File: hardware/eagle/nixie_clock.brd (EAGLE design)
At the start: 273.1 x 130.8 mm, 39 parts, among them IC1 74141N, IC10 74141N, IC11 7477N, IC12 74141N, IC13 7477N, IC14 74AC11238, IC2 7477N, IC4 74141N, IC5 7477N, IC6 74141N, IC7 7477N, IC8 74141N, IC9 7477N

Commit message: First board
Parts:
- removed IC14: 74AC11238, 74ac-logic:DIL16
- added IC3: 74141N, 74xx-eu:DIL16
- added J1_180V, J1_180V1: 22-27-2021-02, con-molex:6410-02
- IC10, IC12, IC4, IC6, IC8: value 74141N -> 7477N; device 74xx-eu:DIL16 -> 74xx-eu:DIL14
- IC11, IC5, IC7, IC9: value 7477N -> 74141N; device 74xx-eu:DIL14 -> 74xx-eu:DIL16
- IC13: value 7477N -> 74AC11238; device 74xx-eu:DIL14 -> 74ac-logic:DIL16
- moved C13 254.8 mm to (118.7, 16.5), turned to 90 degrees
- moved R2 248.9 mm to (5.08, 69.2), turned to 180 degrees
- moved R3 248.9 mm to (5.08, 65.4), turned to 180 degrees
- moved R4 248.9 mm to (5.08, 61.6), turned to 180 degrees
- moved R5 248.9 mm to (5.08, 57.8), turned to 180 degrees
- moved R6 248.9 mm to (5.08, 54.0), turned to 180 degrees
- moved C9 221.2 mm to (41.9, 43.2)
- moved GPIO_HEADER1 220.5 mm to (91.4, 7.62)
- moved C11 217.4 mm to (21.6, 43.2)
- moved IC11 215.8 mm to (22.9, 50.8)
- moved C10 208.9 mm to (59.7, 27.9), turned to 180 degrees
- moved IC13 205.0 mm to (128.3, 14.6), turned to 90 degrees
- moved C12 203.2 mm to (41.9, 27.9), turned to 180 degrees
- moved IN-8-5 198.1 mm to (52.1, 66.0)
- moved IN-8-6 192.8 mm to (35.6, 66.0)
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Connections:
- net +5V: now also IC10.4, IC11.5, IC12.4, IC13.11, IC13.12, IC3.5, IC4.4, IC5.5, IC6.4, IC7.5, IC8.4, IC9.5, J1_180V1.1; no longer IC10.5, IC11.4, IC12.5, IC13.4, IC14.11, IC14.12, IC4.5, IC5.4, IC6.5, IC7.4, IC8.5, IC9.4
- net GND: now also IC10.11, IC11.12, IC12.11, IC13.10, IC13.4, IC13.9, IC3.12, IC4.11, IC5.12, IC6.11, IC7.12, IC8.11, IC9.12, J1_180V.1, J1_180V1.2; no longer IC10.12, IC11.11, IC12.12, IC13.11, IC14.10, IC14.4, IC14.9, IC4.12, IC5.11, IC6.12, IC7.11, IC8.12, IC9.11
- net N$1: now also IN-8-1.A; no longer IN-8-2.A
- net N$10: now also IN-8-1.9; no longer IN-8-2.9
- net N$11: now also IN-8-1.0; no longer IN-8-2.0
- net N$16: now also IC13.16; no longer IC14.16
- net N$17: now also IC10.6, IC12.6, IC4.6, IC6.6, IC8.6; no longer IC11.6, IC13.6, IC5.6, IC7.6, IC9.6
- net N$18: now also IN-8-2.A; no longer IN-8-1.A
- net N$19: now also IC3.15, IN-8-2.1; no longer IC4.15, IN-8-1.1
- net N$2: now also IN-8-1.1; no longer IN-8-2.1
- net N$20: now also IC3.8, IN-8-2.2; no longer IC4.8, IN-8-1.2
- net N$21: now also IC3.9, IN-8-2.3; no longer IC4.9, IN-8-1.3
- net N$22: now also IC3.13, IN-8-2.4; no longer IC4.13, IN-8-1.4
- net N$23: now also IC3.14, IN-8-2.5; no longer IC4.14, IN-8-1.5
- net N$24: now also IC3.11, IN-8-2.6; no longer IC4.11, IN-8-1.6
- net N$25: now also IC3.10, IN-8-2.7; no longer IC4.10, IN-8-1.7
- net N$26: now also IC3.1, IN-8-2.8; no longer IC4.1, IN-8-1.8
- net N$27: now also IC3.2, IN-8-2.9; no longer IC4.2, IN-8-1.9
- net N$28: now also IC3.16, IN-8-2.0; no longer IC4.16, IN-8-1.0
- net N$29: now also IC3.3, IC4.14; no longer IC4.3, IC5.14
- net N$3: now also IN-8-1.2; no longer IN-8-2.2
- net N$30: now also IC3.6, IC4.13; no longer IC4.6, IC5.13
- net N$31: now also IC3.7, IC4.9; no longer IC4.7, IC5.9
- net N$32: now also IC3.4, IC4.8; no longer IC4.4, IC5.8
- net N$33: now also IC13.1, IC4.12, IC4.3; no longer IC14.1, IC5.12, IC5.3
- net N$34: now also IC5.15; no longer IC6.15
- net N$35: now also IC5.8; no longer IC6.8
- net N$36: now also IC5.9; no longer IC6.9
- net N$37: now also IC5.13; no longer IC6.13
- net N$38: now also IC5.14; no longer IC6.14
- net N$39: now also IC5.11; no longer IC6.11
- net N$4: now also IN-8-1.3; no longer IN-8-2.3
- net N$40: now also IC5.10; no longer IC6.10
- net N$41: now also IC5.1; no longer IC6.1
- net N$42: now also IC5.2; no longer IC6.2
- net N$43: now also IC5.16; no longer IC6.16
- net N$44: now also IC5.3, IC6.14; no longer IC6.3, IC7.14
- net N$45: now also IC5.6, IC6.13; no longer IC6.6, IC7.13
- net N$46: now also IC5.7, IC6.9; no longer IC6.7, IC7.9
- net N$47: now also IC5.4, IC6.8; no longer IC6.4, IC7.8
- net N$48: now also IC13.2, IC6.12, IC6.3; no longer IC14.2, IC7.12, IC7.3
- net N$49: now also IC7.15; no longer IC8.15
- net N$5: now also IN-8-1.4; no longer IN-8-2.4
- net N$50: now also IC7.8; no longer IC8.8
- net N$51: now also IC7.9; no longer IC8.9
- net N$52: now also IC7.13; no longer IC8.13
- net N$53: now also IC7.14; no longer IC8.14
- net N$54: now also IC7.11; no longer IC8.11
- net N$55: now also IC7.10; no longer IC8.10
- net N$56: now also IC7.1; no longer IC8.1
- net N$57: now also IC7.2; no longer IC8.2
- net N$58: now also IC7.16; no longer IC8.16
- net N$59: now also IC7.3, IC8.14; no longer IC8.3, IC9.14
- net N$6: now also IN-8-1.5; no longer IN-8-2.5
- net N$60: now also IC7.6, IC8.13; no longer IC8.6, IC9.13
- net N$61: now also IC7.7, IC8.9; no longer IC8.7, IC9.9
- net N$62: now also IC7.4, IC8.8; no longer IC8.4, IC9.8
- net N$63: now also IC13.3, IC8.12, IC8.3; no longer IC14.3, IC9.12, IC9.3
- net N$64: now also IC9.15; no longer IC10.15
- net N$65: now also IC9.8; no longer IC10.8
- net N$66: now also IC9.9; no longer IC10.9
- net N$67: now also IC9.13; no longer IC10.13
- net N$68: now also IC9.14; no longer IC10.14
- net N$69: now also IC9.11; no longer IC10.11
- net N$7: now also IN-8-1.6; no longer IN-8-2.6
- net N$70: now also IC9.10; no longer IC10.10
- net N$71: now also IC9.1; no longer IC10.1
- net N$72: now also IC9.2; no longer IC10.2
- net N$73: now also IC9.16; no longer IC10.16
- net N$74: now also IC10.14, IC9.3; no longer IC10.3, IC11.14
- net N$75: now also IC10.13, IC9.6; no longer IC10.6, IC11.13
- net N$76: now also IC10.9, IC9.7; no longer IC10.7, IC11.9
- net N$77: now also IC10.8, IC9.4; no longer IC10.4, IC11.8
- net N$78: now also IC10.12, IC10.3, IC13.5; no longer IC11.12, IC11.3, IC14.5
- net N$79: now also IC11.15; no longer IC12.15
- net N$8: now also IN-8-1.7; no longer IN-8-2.7
- net N$80: now also IC11.8; no longer IC12.8
- net N$81: now also IC11.9; no longer IC12.9
- net N$82: now also IC11.13; no longer IC12.13
- net N$83: now also IC11.14; no longer IC12.14
- net N$84: now also IC11.11; no longer IC12.11
- net N$85: now also IC11.10; no longer IC12.10
- net N$86: now also IC11.1; no longer IC12.1
- net N$87: now also IC11.2; no longer IC12.2
- net N$88: now also IC11.16; no longer IC12.16
- net N$89: now also IC11.3, IC12.14; no longer IC12.3, IC13.14
- net N$9: now also IN-8-1.8; no longer IN-8-2.8
- net N$90: now also IC11.6, IC12.13; no longer IC12.6, IC13.13
- net N$91: now also IC11.7, IC12.9; no longer IC12.7, IC13.9
- net N$92: now also IC11.4, IC12.8; no longer IC12.4, IC13.8
- net N$93: now also IC12.12, IC12.3, IC13.6; no longer IC13.12, IC13.3, IC14.6
- net N$94: now also IC10.5, IC12.5, IC4.5, IC6.5, IC8.5; no longer IC11.5, IC13.5, IC5.5, IC7.5, IC9.5
- net N$95: now also IC10.2, IC12.2, IC4.2, IC6.2, IC8.2; no longer IC11.2, IC13.2, IC5.2, IC7.2, IC9.2
- net N$96: now also IC10.1, IC12.1, IC4.1, IC6.1, IC8.1; no longer IC11.1, IC13.1, IC5.1, IC7.1, IC9.1
- net N$97: now also IC13.15; no longer IC14.15
- net N$98: now also IC13.14; no longer IC14.14
- net N$99: now also IC13.13; no longer IC14.13
- net VCC: now also J1_180V.2
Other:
- board size 273.1 x 130.8 mm -> 138.4 x 74.9 mm

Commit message: Updated eagle project
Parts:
- removed J1_180V1: 22-27-2021-02, con-molex:6410-02
- added J1_5V1: 22-27-2021-02, con-molex:6410-02
- R1, R2, R3, R4, R5, R6: device resistor:0204/5 -> resistor:0207/15
- moved R1 65.9 mm to (33.0, 12.7), turned to 270 degrees
- moved R2 61.5 mm to (29.2, 12.7), turned to 270 degrees
- moved R3 56.5 mm to (25.4, 12.7), turned to 270 degrees
- moved J1_180V 53.6 mm to (48.3, 14.0), turned to 0 degrees
- moved R4 51.6 mm to (21.6, 12.7), turned to 270 degrees
- moved R5 46.8 mm to (17.8, 12.7), turned to 270 degrees
- moved R6 42.2 mm to (14.0, 12.7), turned to 270 degrees
- moved C12 25.4 mm to (16.5, 27.9), turned to 0 degrees
- moved C10 24.1 mm to (35.6, 27.9), turned to 0 degrees
- moved IN-8-6 22.9 mm to (12.7, 66.0)
- moved IC12 19.0 mm to (17.8, 35.6)
- moved IN-8-5 19.0 mm to (33.0, 66.0)
- moved IC10 17.8 mm to (36.8, 35.6)
- moved C8 15.2 mm to (62.2, 27.9), turned to 0 degrees
- moved C6 14.0 mm to (81.3, 27.9), turned to 0 degrees
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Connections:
- new net N$108: C1.2, C10.2, C11.2, C12.2, C13.2, C2.2, C3.2, C4.2, C5.2, C6.2, C7.2, C8.2, C9.2, IC1.5, IC10.4, IC11.5, IC12.4, IC13.11, IC13.12, IC2.4, IC3.5, IC4.4, IC5.5, IC6.4, IC7.5, IC8.4, IC9.5, J1_5V1.2
- net +5V: no longer C1.2, C10.2, C11.2, C12.2, C13.2, C2.2, C3.2, C4.2, C5.2, C6.2, C7.2, C8.2, C9.2, IC1.5, IC10.4, IC11.5, IC12.4, IC13.11, IC13.12, IC2.4, IC3.5, IC4.4, IC5.5, IC6.4, IC7.5, IC8.4, IC9.5, J1_180V1.1
- net GND: now also J1_5V1.1; no longer J1_180V1.2
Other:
- board size 138.4 x 74.9 mm -> 141 x 74.9 mm

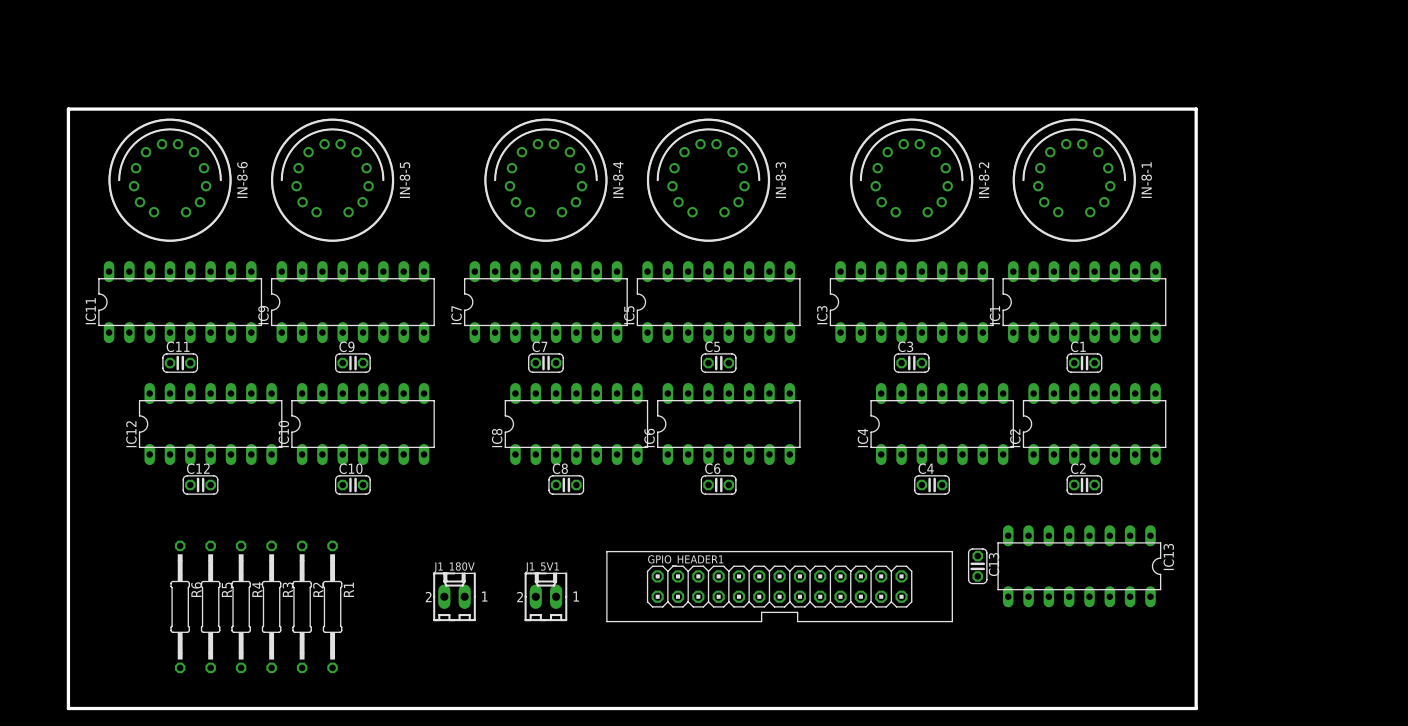
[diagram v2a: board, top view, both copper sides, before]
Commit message: External nixie tubes design
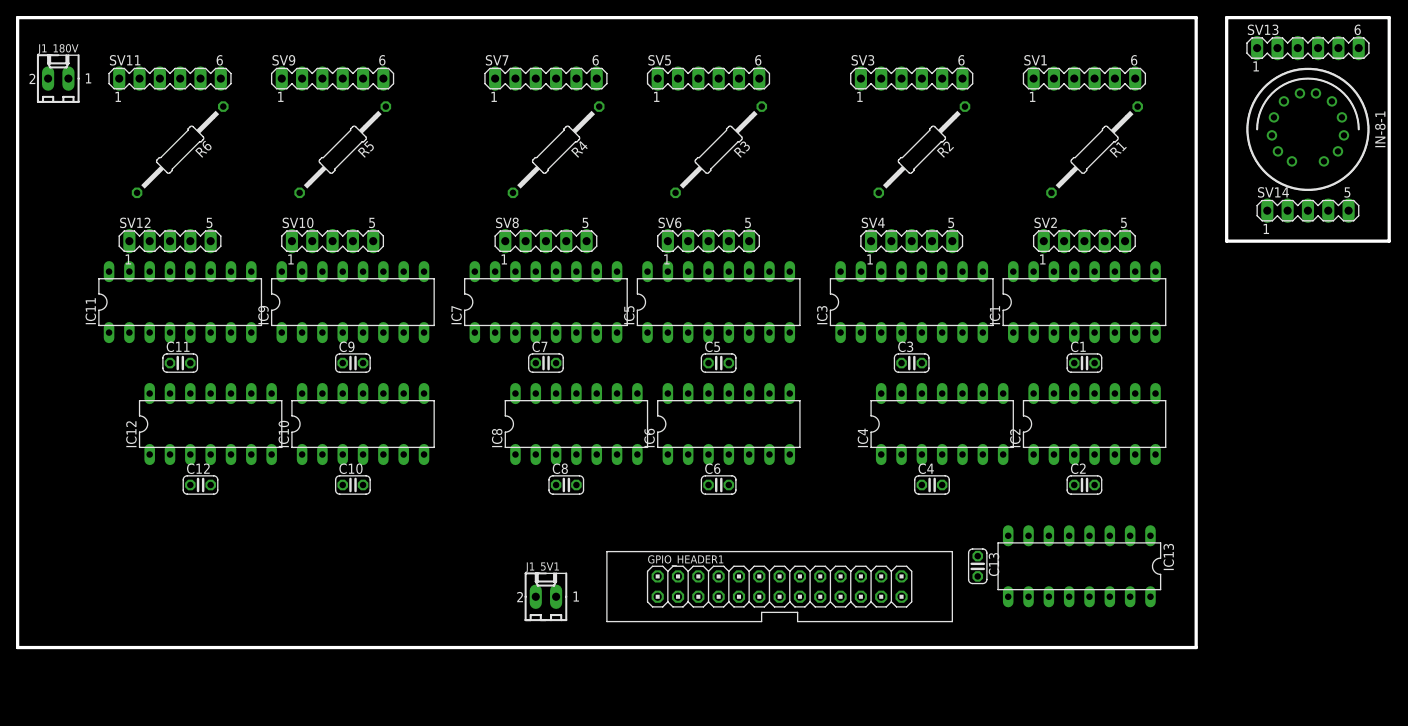
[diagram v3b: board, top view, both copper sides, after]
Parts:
- removed IN-8-2, IN-8-3, IN-8-4, IN-8-5, IN-8-6: IN-8-2, russian-nixies:IN-8-2
- added SV1, SV11, SV13, SV3, SV5, SV7, SV9: (no value), con-lstb:MA06-1
- added SV10, SV12, SV14, SV2, SV4, SV6, SV8: (no value), con-lstb:MA05-1
- moved R1 111.1 mm to (128.3, 69.8), turned to 225 degrees
- moved R2 96.3 mm to (106.7, 69.8), turned to 225 degrees
- moved J1_180V 81.5 mm to (-1.27, 78.7)
- moved R3 79.9 mm to (81.3, 69.8), turned to 225 degrees
- moved R4 69.4 mm to (61.0, 69.8), turned to 225 degrees
- moved R5 59.5 mm to (34.3, 69.8), turned to 225 degrees
- moved R6 57.1 mm to (14.0, 69.8), turned to 225 degrees
- moved IN-8-1 29.9 mm to (154.9, 72.4)
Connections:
- new net N$104: IN-8-1.1, SV14.2
- new net N$105: IN-8-1.2, SV14.3
- new net N$106: IN-8-1.3, SV14.4
- new net N$107: IN-8-1.4, SV14.5
- new net N$109: IN-8-1.5, SV13.1
- new net N$110: IN-8-1.6, SV13.2
- new net N$111: IN-8-1.7, SV13.3
- new net N$112: IN-8-1.8, SV13.4
- new net N$113: IN-8-1.9, SV13.5
- new net N$114: IN-8-1.0, SV14.1
- new net N$115: IN-8-1.A, SV13.6
- net N$1: now also IC3.14, SV3.1; no longer IN-8-1.A, R1.1
- net N$10: now also IC1.1, SV1.4; no longer IC1.2, IN-8-1.9
- net N$100: now also R3.1, SV5.6; no longer IN-8-4.A, R4.1
- net N$101: now also R4.1, SV7.6; no longer IN-8-5.A, R5.1
- net N$102: now also R5.1, SV9.6; no longer IN-8-6.A, R6.1
- net N$103: now also R6.1, SV11.6; no longer IN-8-3.A, R3.1
- net N$11: now also IC1.2, SV1.5; no longer IC1.16, IN-8-1.0
- net N$18: now also IC3.1, SV3.4; no longer IN-8-2.A, R2.1
- net N$19: now also IC3.16, SV4.1; no longer IC3.15, IN-8-2.1
- net N$2: now also IC1.16, SV2.1; no longer IC1.15, IN-8-1.1
- net N$20: now also IC3.15, SV4.2; no longer IC3.8, IN-8-2.2
- net N$21: now also IC3.8, SV4.3; no longer IC3.9, IN-8-2.3
- net N$22: now also IC3.9, SV4.4; no longer IC3.13, IN-8-2.4
- net N$23: now also IC3.13, SV4.5; no longer IC3.14, IN-8-2.5
- net N$24: now also IC7.14, SV7.1; no longer IC3.11, IN-8-2.6
- net N$25: now also IC7.11, SV7.2; no longer IC3.10, IN-8-2.7
- net N$26: now also IC7.10, SV7.3; no longer IC3.1, IN-8-2.8
- net N$27: now also IC7.1, SV7.4; no longer IC3.2, IN-8-2.9
- net N$28: now also IC7.2, SV7.5; no longer IC3.16, IN-8-2.0
- net N$3: now also IC1.15, SV2.2; no longer IC1.8, IN-8-1.2
- net N$34: now also IC5.16, SV6.1; no longer IC5.15, IN-8-3.1
- net N$35: now also IC5.15, SV6.2; no longer IC5.8, IN-8-3.2
- net N$36: now also IC5.8, SV6.3; no longer IC5.9, IN-8-3.3
- net N$37: now also IC5.9, SV6.4; no longer IC5.13, IN-8-3.4
- net N$38: now also IC5.13, SV6.5; no longer IC5.14, IN-8-3.5
- net N$39: now also IC9.14, SV9.1; no longer IC5.11, IN-8-3.6
- net N$4: now also IC1.8, SV2.3; no longer IC1.9, IN-8-1.3
- net N$40: now also IC9.11, SV9.2; no longer IC5.10, IN-8-3.7
- net N$41: now also IC9.10, SV9.3; no longer IC5.1, IN-8-3.8
- net N$42: now also IC9.1, SV9.4; no longer IC5.2, IN-8-3.9
- net N$43: now also IC9.2, SV9.5; no longer IC5.16, IN-8-3.0
- net N$49: now also IC7.16, SV8.1; no longer IC7.15, IN-8-4.1
- net N$5: now also IC1.9, SV2.4; no longer IC1.13, IN-8-1.4
- net N$50: now also IC7.15, SV8.2; no longer IC7.8, IN-8-4.2
- net N$51: now also IC7.8, SV8.3; no longer IC7.9, IN-8-4.3
- net N$52: now also IC7.9, SV8.4; no longer IC7.13, IN-8-4.4
- net N$53: now also IC7.13, SV8.5; no longer IC7.14, IN-8-4.5
- net N$54: now also IC11.14, SV11.1; no longer IC7.11, IN-8-4.6
- net N$55: now also IC11.11, SV11.2; no longer IC7.10, IN-8-4.7
- net N$56: now also IC11.10, SV11.3; no longer IC7.1, IN-8-4.8
- net N$57: now also IC11.1, SV11.4; no longer IC7.2, IN-8-4.9
- net N$58: now also IC11.2, SV11.5; no longer IC7.16, IN-8-4.0
- net N$6: now also IC1.13, SV2.5; no longer IC1.14, IN-8-1.5
- net N$64: now also IC9.16, SV10.1; no longer IC9.15, IN-8-5.1
- net N$65: now also IC9.15, SV10.2; no longer IC9.8, IN-8-5.2
- net N$66: now also IC9.8, SV10.3; no longer IC9.9, IN-8-5.3
- net N$67: now also IC9.9, SV10.4; no longer IC9.13, IN-8-5.4
- net N$68: now also IC9.13, SV10.5; no longer IC9.14, IN-8-5.5
- net N$69: now also IC3.11, SV3.2; no longer IC9.11, IN-8-5.6
- net N$7: now also IC1.14, SV1.1; no longer IC1.11, IN-8-1.6
- net N$70: now also IC3.10, SV3.3; no longer IC9.10, IN-8-5.7
- net N$71: now also IC3.2, SV3.5; no longer IC9.1, IN-8-5.8
- net N$72: now also R2.1, SV3.6; no longer IC9.2, IN-8-5.9
- net N$73: now also R1.1, SV1.6; no longer IC9.16, IN-8-5.0
- net N$79: now also IC11.16, SV12.1; no longer IC11.15, IN-8-6.1
- net N$8: now also IC1.11, SV1.2; no longer IC1.10, IN-8-1.7
- net N$80: now also IC11.15, SV12.2; no longer IC11.8, IN-8-6.2
- net N$81: now also IC11.8, SV12.3; no longer IC11.9, IN-8-6.3
- net N$82: now also IC11.9, SV12.4; no longer IC11.13, IN-8-6.4
- net N$83: now also IC11.13, SV12.5; no longer IC11.14, IN-8-6.5
- net N$84: now also IC5.14, SV5.1; no longer IC11.11, IN-8-6.6
- net N$85: now also IC5.11, SV5.2; no longer IC11.10, IN-8-6.7
- net N$86: now also IC5.10, SV5.3; no longer IC11.1, IN-8-6.8
- net N$87: now also IC5.1, SV5.4; no longer IC11.2, IN-8-6.9
- net N$88: now also IC5.2, SV5.5; no longer IC11.16, IN-8-6.0
- net N$9: now also IC1.10, SV1.3; no longer IC1.1, IN-8-1.8
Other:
- board size 141 x 74.9 mm -> 171.4 x 78.7 mm

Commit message: Updated eagle project
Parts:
- moved R1 14.2 mm to (125.7, 83.8), turned to 180 degrees
- moved R6 14.2 mm to (11.4, 83.8), turned to 180 degrees
- moved R2 14.0 mm to (105.4, 83.8), turned to 180 degrees
- moved R3 14.0 mm to (80.0, 83.8), turned to 180 degrees
- moved R4 14.0 mm to (59.7, 83.8), turned to 180 degrees
- moved R5 14.0 mm to (33.0, 83.8), turned to 180 degrees
- moved J1_5V1 9.67 mm to (50.8, 17.8), turned to 180 degrees
- moved J1_180V 6.35 mm to (-1.27, 72.4)
- moved GPIO_HEADER1 2.84 mm to (87.6, 17.8)
- moved C13 1.80 mm to (112.4, 19.1)
- moved IC13 1.27 mm to (126.4, 19.1)
- moved SV11 1.27 mm to (11.4, 78.7)
- moved SV12 1.27 mm to (11.4, 58.4)
- moved SV1 1.27 mm to (125.7, 78.7)
- moved SV2 1.27 mm to (125.7, 58.4)
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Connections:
- removed net N$105 (its old number): IN-8-1.2, SV14.3
- removed net N$19 (its old number): IC3.16, SV4.1
- removed net N$2 (its old number): IC1.16, SV2.1
- removed net N$4 (its old number): IC1.8, SV2.3
- removed net N$5 (its old number): IC1.9, SV2.4
- removed net N$51 (its old number): IC7.8, SV8.3
- removed net N$67 (its old number): IC9.9, SV10.4
- removed net N$7 (its old number): IC1.14, SV1.1
- removed net N$84 (its old number): IC5.14, SV5.1
- new net N$104: IN-8-1.A, SV14.3
- new net N$12: IC1.13, SV1.2
- new net N$13: IC1.14, SV1.3
- new net N$14: IC1.11, SV1.4
- new net N$15: IC1.10, SV1.5
- new net N$20: IC3.16, SV4.4
- new net N$50: IC7.8, SV8.1
- new net N$65: R5.1, SV10.3
- new net N$80: IC9.10, SV9.5
- net N$1: now also R2.1, SV4.3; no longer IC3.14, SV3.1
- net N$10: now also IC1.2, SV2.5; no longer IC1.1, SV1.4
- net N$100: now also IC11.14, SV11.3; no longer R3.1, SV5.6
- net N$101: now also IC11.11, SV11.4; no longer R4.1, SV7.6
- net N$102: now also IC11.10, SV11.5; no longer R5.1, SV9.6
- net N$103: now also IC11.1; no longer R6.1
- net N$106: now also IN-8-1.2, SV14.1; no longer IN-8-1.3, SV14.4
- net N$107: now also IN-8-1.0, SV14.4; no longer IN-8-1.4, SV14.5
- net N$109: now also IN-8-1.9, SV14.5; no longer IN-8-1.5, SV13.1
- net N$11: now also IC1.9, SV1.1; no longer IC1.2, SV1.5
- net N$110: now also IN-8-1.8, SV13.6; no longer IN-8-1.6, SV13.2
- net N$111: now also SV13.5; no longer SV13.3
- net N$112: now also IN-8-1.6; no longer IN-8-1.8
- net N$113: now also IN-8-1.5, SV13.3; no longer IN-8-1.9, SV13.5
- net N$114: now also IN-8-1.4, SV13.2; no longer IN-8-1.0, SV14.1
- net N$115: now also IN-8-1.3, SV13.1; no longer IN-8-1.A, SV13.6
- net N$18: now also IC3.8, SV4.1; no longer IC3.1, SV3.4
- net N$21: now also IC3.2, SV4.5; no longer IC3.8, SV4.3
- net N$22: now also SV3.1; no longer SV4.4
- net N$23: now also SV3.2; no longer SV4.5
- net N$24: now also IC3.14, SV3.3; no longer IC7.14, SV7.1
- net N$25: now also IC3.11, SV3.4; no longer IC7.11, SV7.2
- net N$26: now also IC3.10, SV3.5; no longer IC7.10, SV7.3
- net N$27: now also IC3.1, SV3.6; no longer IC7.1, SV7.4
- net N$28: now also R3.1, SV6.3; no longer IC7.2, SV7.5
- net N$34: now also IC5.8; no longer IC5.16
- net N$36: now also IC5.16, SV6.4; no longer IC5.8, SV6.3
- net N$37: now also IC5.2, SV6.5; no longer IC5.9, SV6.4
- net N$38: now also IC5.9, SV5.1; no longer IC5.13, SV6.5
- net N$39: now also IC5.13, SV5.2; no longer IC9.14, SV9.1
- net N$40: now also IC5.14, SV5.3; no longer IC9.11, SV9.2
- net N$41: now also IC5.11, SV5.4; no longer IC9.10, SV9.3
- net N$42: now also IC5.10, SV5.5; no longer IC9.1, SV9.4
- net N$43: now also IC5.1, SV5.6; no longer IC9.2, SV9.5
- net N$49: now also R4.1, SV8.3; no longer IC7.16, SV8.1
- net N$52: now also IC7.16; no longer IC7.9
- net N$53: now also IC7.2; no longer IC7.13
- net N$54: now also IC7.9, SV7.1; no longer IC11.14, SV11.1
- net N$55: now also IC7.13, SV7.2; no longer IC11.11, SV11.2
- net N$56: now also IC7.14, SV7.3; no longer IC11.10, SV11.3
- net N$57: now also IC7.11, SV7.4; no longer IC11.1, SV11.4
- net N$58: now also IC7.10, SV7.5; no longer IC11.2, SV11.5
- net N$6: now also R1.1, SV2.3; no longer IC1.13, SV2.5
- net N$64: now also IC7.1, SV7.6; no longer IC9.16, SV10.1
- net N$66: now also SV10.1; no longer SV10.3
- net N$68: now also IC9.16, SV10.4; no longer IC9.13, SV10.5
- net N$69: now also IC9.2, SV10.5; no longer IC3.11, SV3.2
- net N$70: now also IC9.9, SV9.1; no longer IC3.10, SV3.3
- net N$71: now also IC9.13, SV9.2; no longer IC3.2, SV3.5
- net N$72: now also IC9.14, SV9.3; no longer R2.1, SV3.6
- net N$73: now also IC1.1; no longer R1.1
- net N$79: now also IC9.11, SV9.4; no longer IC11.16, SV12.1
- net N$8: now also IC1.8, SV2.1; no longer IC1.11, SV1.2
- net N$81: now also IC9.1, SV9.6; no longer IC11.8, SV12.3
- net N$82: now also R6.1, SV12.3; no longer IC11.9, SV12.4
- net N$83: now also IC11.8, SV12.1; no longer IC11.13, SV12.5
- net N$85: now also IC11.16, SV12.4; no longer IC5.11, SV5.2
- net N$86: now also IC11.2, SV12.5; no longer IC5.10, SV5.3
- net N$87: now also IC11.9, SV11.1; no longer IC5.1, SV5.4
- net N$88: now also IC11.13, SV11.2; no longer IC5.2, SV5.5
- net N$9: now also IC1.16, SV2.4; no longer IC1.10, SV1.3
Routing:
- net GND: track 0.00 -> 603.0 mm, vias 0 -> 1
- net N$108: track 0.00 -> 337.5 mm
- net N$95: track 0.00 -> 185.6 mm, vias 0 -> 2
- net N$17: track 0.00 -> 169.7 mm, vias 0 -> 2
- net N$94: track 0.00 -> 160.3 mm, vias 0 -> 2
- net VCC: track 0.00 -> 134.6 mm
- net N$96: track 0.00 -> 133.1 mm
- net N$93: track 0.00 -> 125.1 mm
- net N$78: track 0.00 -> 122.9 mm, vias 0 -> 2
- net N$63: track 0.00 -> 84.8 mm
- net N$48: track 0.00 -> 64.0 mm
- net N$64: track 0.00 -> 56.7 mm
- net N$27: track 0.00 -> 50.8 mm
- net N$43: track 0.00 -> 49.5 mm
- net N$98: track 0.00 -> 48.2 mm
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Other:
- outline, holes or cut-outs redrawn
